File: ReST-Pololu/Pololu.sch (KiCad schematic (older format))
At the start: 12 parts, among them P1 02X07-MALE, P2 01X03-MALE, P3 03-SCREW-TERM, P4 01X03-MALE, P5 02-SCREW-TERM, P6 02X04-MALE, P7 02X03-MALE, U1 POLOLU_A4988

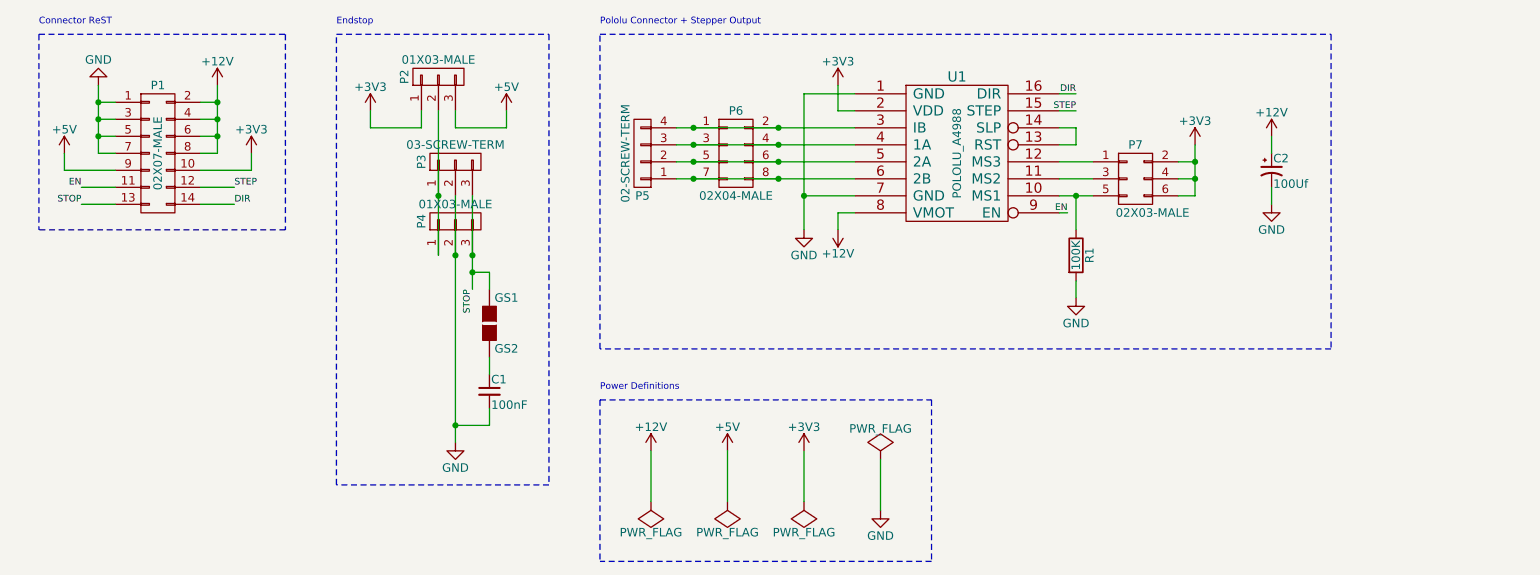
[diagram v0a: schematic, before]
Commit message: Added Pololu Driver PCB
Size is 3.5cm * 3.75cm
Im pretty happy with that size
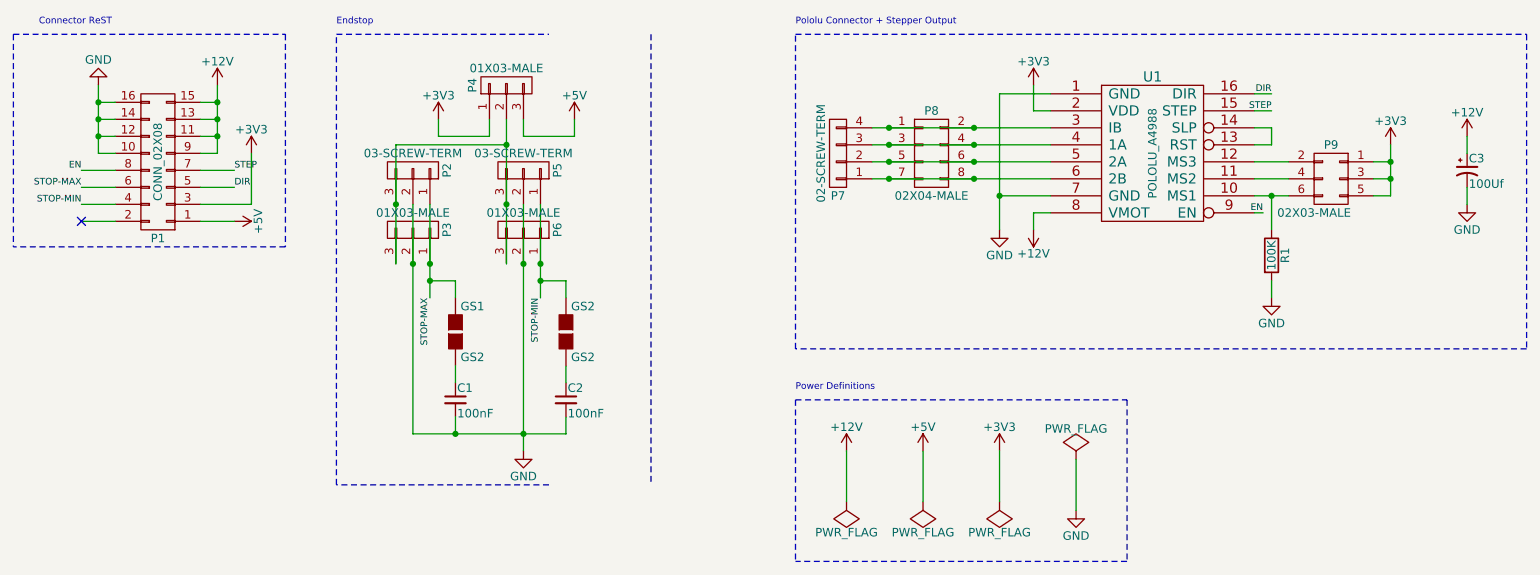
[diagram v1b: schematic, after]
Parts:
- removed P1: 02X07-MALE, Pin_Headers:Pin_Header_Angled_2x07, symbol CONN_02X07
- added C1: 100nF, ok-smd-generic:1206, symbol C_Small
- added GS1: GS2, Connect:GS2, symbol GS2
- added P1: CONN_02X08, Pin_Headers:Pin_Header_Angled_2x08, symbol CONN_02X08
- added P2: 03-SCREW-TERM, 2:mpt_0,5%2f3-2,54, symbol CONN_01X03
- added P3: 01X03-MALE, Pin_Headers:Pin_Header_Straight_1x03, symbol CONN_01X03
- renumbered C1 to C2, C2 to C3, GS1 to GS2, P2 to P4, P3 to P5, P4 to P6, P5 to P7, P6 to P8, P7 to P9
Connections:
- net +12V: now also P1.11 (P11), P1.13 (P13), P1.15 (P15), P1.9 (P9)
- net +3V3: now also P9.1 (P1), P9.3 (P3), P9.5 (P5), P1.3 (P3); no longer P9.2 (P2), P9.4 (P4), P9.6 (P6)
- net +5V: now also P1.1 (P1)
- net DIR: now also P1.5 (P5)
- net EN: now also P1.8 (P8)
- net GND: now also C1.2, P1.10 (P10), P1.12 (P12), P1.14 (P14), P1.16 (P16), P2.2 (P2), P3.2 (P2)
- net STEP: now also P1.7 (P7)
- net at R1.1, U1.10 (MS1): now also P9.6 (P6); no longer P9.5 (P5)
- net at U1.11 (MS2): now also P9.4 (P4); no longer P9.3 (P3)
- net at U1.12 (MS3): now also P9.2 (P2); no longer P9.1 (P1)
- net STOP-MIN: now reaches P5.1 (P1), P6.1 (P1)
- net STOP-MIN: now also GS2.1 (G1), P1.4 (P4); no longer P4.2 (P2)
- net STOP: no longer names the net of P5.3 (P3), P6.3 (P3)
- net STOP: now also P4.2 (P2), P2.3 (P3), P3.3 (P3); no longer GS2.1 (G1)
- new net: C1.1, GS1.2 (G2)
- new net STOP-MAX: GS1.1 (G1), P1.6 (P6), P2.1 (P1), P3.1 (P1)
- no-connect marks 0 -> 1
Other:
- moved on the sheet: C2, C3, GS2, P4, P5, P6, P7, P8, P9, R1, U1

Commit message: Changed minor issues in the Pololu Driver.
Heatbed wont get much smaller. Finished Dimensions:
Heatbed: 30,4mm * 47,8mm
Heater: 29mm * 34,1mm
Pololu: 36,3mm * 35,2mm
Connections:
- net +12V: now also P1.10 (P10), P1.12 (P12), P1.14 (P14), P1.16 (P16); no longer P1.11 (P11), P1.13 (P13), P1.15 (P15), P1.9 (P9)
- net GND: now also P1.11 (P11), P1.13 (P13), P1.15 (P15), P1.9 (P9); no longer P1.10 (P10), P1.12 (P12), P1.14 (P14), P1.16 (P16)
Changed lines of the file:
@@
 L +12V #PWR01
 U 1 1 56A92F1E
-P 1850 1350
-F 0 "#PWR01" H 1850 1200 50  0001 C CNN
-F 1 "+12V" H 1850 1490 50  0000 C CNN
-F 2 "" H 1850 1350 50  0000 C CNN
-F 3 "" H 1850 1350 50  0000 C CNN
-	1    1850 1350
+P 1150 1350
+F 0 "#PWR01" H 1150 1200 50  0001 C CNN
+F 1 "+12V" H 1150 1490 50  0000 C CNN
+F 2 "" H 1150 1350 50  0000 C CNN
+F 3 "" H 1150 1350 50  0000 C CNN
+	1    1150 1350
 	1    0    0    -1
 $EndComp
@@
 L GND #PWR03
 U 1 1 56A92F64
-P 1150 1350
-F 0 "#PWR03" H 1150 1100 50  0001 C CNN
-F 1 "GND" H 1150 1200 50  0000 C CNN
-F 2 "" H 1150 1350 50  0000 C CNN
-F 3 "" H 1150 1350 50  0000 C CNN
-	1    1150 1350
+P 1850 1350
+F 0 "#PWR03" H 1850 1100 50  0001 C CNN
+F 1 "GND" H 1850 1200 50  0000 C CNN
+F 2 "" H 1850 1350 50  0000 C CNN
+F 3 "" H 1850 1350 50  0000 C CNN
+	1    1850 1350
 	-1   0    0    1
 $EndComp
@@
 $EndComp
 Wire Wire Line
-	1850 1350 1850 1750
-Wire Wire Line
 	1850 1450 1750 1450
 Wire Wire Line
@@
 Connection ~ 1850 1650
 Wire Wire Line
-	1750 1550 1850 1550
+	1850 1550 1750 1550
 Connection ~ 1850 1550
 Wire Wire Line
@@
 Connection ~ 5800 1900
 Wire Wire Line
-	1150 1350 1150 1750
-Wire Wire Line
 	3550 1550 3550 2400
 Wire Wire Line
@@
 Wire Wire Line
 	1950 2150 1750 2150
+Wire Wire Line
+	1850 1350 1850 1750
+Wire Wire Line
+	1150 1350 1150 1750
 $EndSCHEMATC
